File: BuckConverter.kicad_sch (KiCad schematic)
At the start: 9 parts, among them U1 TPS56339DDC

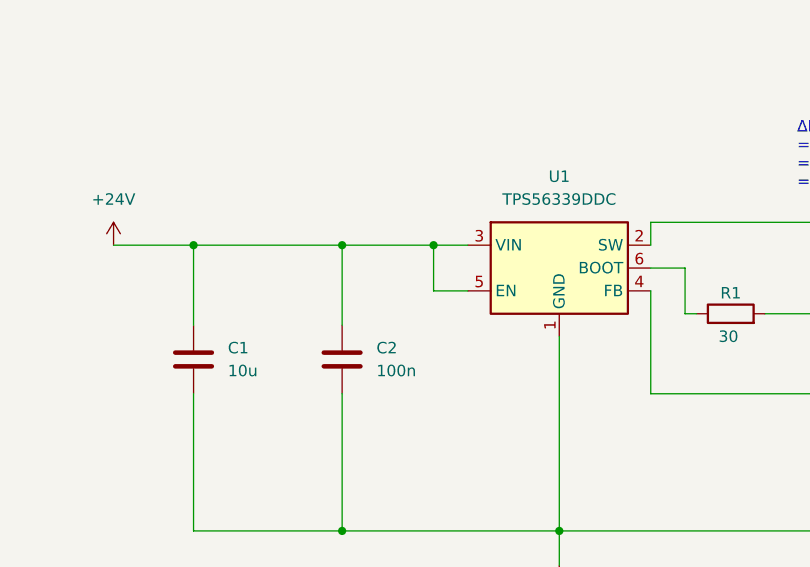
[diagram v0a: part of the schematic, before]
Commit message: added testpoints too
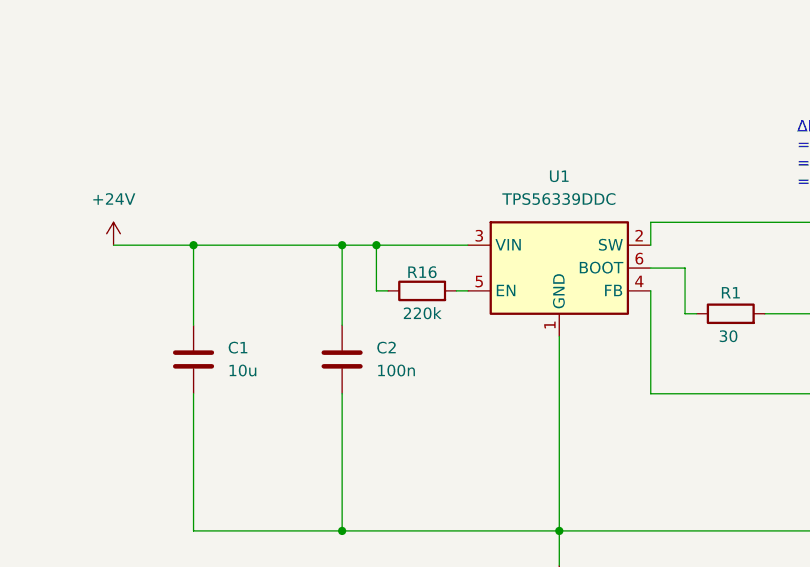
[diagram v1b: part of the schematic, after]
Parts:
- added R16: 220k, symbol Device:R
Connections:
- net +24V: now also R16.1; no longer U1.5 (EN)
- new net: R16.2, U1.5 (EN)
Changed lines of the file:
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@@
+	)
+	(junction
+		(at 104.14 72.39)
+		(diameter 0)
+		(color 0 0 0 0)
 	)
 	(junction
@@
 	)
 	(junction
-		(at 110.49 72.39)
-		(diameter 0)
-		(color 0 0 0 0)
-	)
-	(junction
 		(at 181.61 72.39)
 		(diameter 0)
@@
 	(wire
 		(pts
-			(xy 114.3 77.47) (xy 110.49 77.47)
+			(xy 114.3 77.47) (xy 113.03 77.47)
 		)
 		(stroke
@@
 	(wire
 		(pts
+			(xy 104.14 72.39) (xy 104.14 77.47)
+		)
+		(stroke
+			(width 0)
+			(type default)
+		)
+	)
+	(wire
+		(pts
 			(xy 74.93 72.39) (xy 83.82 72.39)
 		)
@@
 	(wire
 		(pts
+			(xy 104.14 72.39) (xy 114.3 72.39)
+		)
+		(stroke
+			(width 0)
+			(type default)
+		)
+	)
+	(wire
+		(pts
 			(xy 83.82 72.39) (xy 100.33 72.39)
 		)
@@
 	(wire
 		(pts
-			(xy 110.49 72.39) (xy 114.3 72.39)
-		)
-		(stroke
-			(width 0)
-			(type default)
-		)
-	)
-	(wire
-		(pts
 			(xy 162.56 80.01) (xy 162.56 74.93)
 		)
@@
 	(wire
 		(pts
-			(xy 100.33 72.39) (xy 110.49 72.39)
+			(xy 100.33 72.39) (xy 104.14 72.39)
 		)
 		(stroke
@@
 	(wire
 		(pts
+			(xy 105.41 77.47) (xy 104.14 77.47)
+		)
+		(stroke
+			(width 0)
+			(type default)
+		)
+	)
+	(wire
+		(pts
 			(xy 134.62 69.85) (xy 134.62 72.39)
 		)
@@
 		(pts
 			(xy 160.02 80.01) (xy 162.56 80.01)
-		)
-		(stroke
-			(width 0)
-			(type default)
-		)
-	)
-	(wire
-		(pts
-			(xy 110.49 77.47) (xy 110.49 72.39)
 		)
 		(stroke
@@
 					(unit 1)
 				)
+			)
+		)
+	)
+	(symbol
+		(lib_id "Device:R")
+		(at 109.22 77.47 90)
+		(unit 1)
+		(exclude_from_sim no)
+		(in_bom yes)
+		(on_board yes)
+		(dnp no)
+		(property "Reference" "R16"
+			(at 109.22 75.438 90)
+			(effects
+				(font
+					(size 1.27 1.27)
+				)
+			)
+		)
+		(property "Value" "220k"
+			(at 109.22 80.01 90)
+			(effects
+				(font
+					(size 1.27 1.27)
+				)
+			)
+		)
+		(property "Footprint" ""
+			(at 109.22 79.248 90)
+			(effects
+				(font
+					(size 1.27 1.27)
+				)
+				(hide yes)
+			)
+		)
+		(property "Datasheet" "~"
+			(at 109.22 77.47 0)
+			(effects
+				(font
+					(size 1.27 1.27)
+				)
+				(hide yes)
+			)
+		)
+		(property "Description" "Resistor"
+			(at 109.22 77.47 0)
+			(effects
+				(font
+					(size 1.27 1.27)
+				)
+				(hide yes)
+			)
+		)
+		(pin "1"
+		)
+		(pin "2"
+		)
+		(instances
+			(project ""
+				(path "/a2e13c19-ff3a-4e43-a7f5-200fd5b2b978/2c6af1c6-af26-4746-8ed9-5deb88ce0ee1"
+					(reference "R16")
+					(unit 1)
+				)

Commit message: changes + ioc
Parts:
- added C18, C3: 22u, symbol Device:C
- L1: value 20u -> 6.8u
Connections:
- net GND: now also C18.2, C3.2; no longer C17.1, L1.2, R2.1
- new net 12V_BUS: C17.1, C18.1, C3.1, L1.2, R2.1
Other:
- note removed: "L = (24-12)(12/24)/(0.8(500,000)) = 6/(400,000) = 15uH"
- note removed: "Vin = 24V Vout = 12V Fsw = 500,000 Hz (typ)"
- note removed: "Vref = .802V (typ) R9 = 10k R2 = R9(Vout - Vref)/Vref R2 = 10k(12-.802)/.802 = 140k"
- note removed: "ΔIL = 0.4(Iout) = 0.4(2A) = 0.8A"
- moved on the sheet: C1, C16, C17, C2, L1, R1, R16, R2, R9, U1

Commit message: layout
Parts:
- C1: footprint (none) -> Capacitor_SMD:C_0805_2012Metric_Pad1.18x1.45mm_HandSolder; Manufacturer_Part_Number (none) -> GRM21BR61H106KE43K
- C16, C2: footprint (none) -> Capacitor_SMD:C_0603_1608Metric_Pad1.08x0.95mm_HandSolder; Manufacturer_Part_Number (none) -> MLASH168SB7104KTNA01
- C17, C18, C3: footprint (none) -> Capacitor_SMD:C_0805_2012Metric_Pad1.18x1.45mm_HandSolder
- L1: footprint (none) -> Inductor_SMD:L_6.3x6.3_H3
- R1, R16, R2: footprint (none) -> Resistor_SMD:R_0603_1608Metric_Pad0.98x0.95mm_HandSolder
- R9: footprint (none) -> Resistor_SMD:R_0603_1608Metric_Pad0.98x0.95mm_HandSolder; Manufacturer_Part_Number (none) -> CRCW060310K0FKEI

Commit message: hello
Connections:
- net SW: now reaches C16.2, L1.1, U1.2 (SW)
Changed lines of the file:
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@@
+		)
+	)
+	(label "SW"
+		(at 132.08 92.71 0)
+		(effects
+			(font
+				(size 1.27 1.27)
+			)
+			(justify left bottom)
 		)
 	)

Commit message: done
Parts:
- L1: Mouser Part Number (none) -> 80-MPEV1D0630L6R8
- U1: Mouser Part Number (none) -> 595-TPS56339DDCR
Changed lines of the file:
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@@
+			)
+		)
+		(property "Sim.Type" ""
+			(at 175.26 115.57 0)
+			(effects
+				(font
+					(size 1.27 1.27)
+				)
+				(hide yes)
 			)
 		)
@@
 			)
 		)
+		(property "Sim.Type" ""
+			(at 93.98 107.95 0)
+			(effects
+				(font
+					(size 1.27 1.27)
+				)
+				(hide yes)
+			)
+		)
 		(pin "1"
 		)
@@
 		)
 		(property "Mouser Link" ""
+			(at 102.87 100.33 90)
+			(effects
+				(font
+					(size 1.27 1.27)
+				)
+				(hide yes)
+			)
+		)
+		(property "Sim.Type" ""
 			(at 102.87 100.33 90)
 			(effects
@@
 			)
 		)
+		(property "Sim.Type" ""
+			(at 175.26 102.87 0)
+			(effects
+				(font
+					(size 1.27 1.27)
+				)
+				(hide yes)
+			)
+		)
 		(pin "1"
 		)
@@
 			)
 		)
+		(property "Sim.Type" ""
+			(at 190.5 107.95 0)
+			(effects
+				(font
+					(size 1.27 1.27)
+				)
+				(hide yes)
+			)
+		)
 		(pin "1"
 		)
@@
 			)
 		)
+		(property "Sim.Type" ""
+			(at 215.9 107.95 0)
+			(effects
+				(font
+					(size 1.27 1.27)
+				)
+				(hide yes)
+			)
+		)
 		(pin "1"
 		)
@@
 			)
 		)
+		(property "Sim.Type" ""
+			(at 137.16 100.33 90)
+			(effects
+				(font
+					(size 1.27 1.27)
+				)
+				(hide yes)
+			)
+		)
 		(pin "2"
 		)
@@
 			)
 		)
+		(property "Sim.Type" ""
+			(at 118.11 97.79 0)
+			(effects
+				(font
+					(size 1.27 1.27)
+				)
+				(hide yes)
+			)
+		)
+		(property "Mouser Part Number" "595-TPS56339DDCR"
+			(at 118.11 97.79 0)
+			(effects
+				(font
+					(size 1.27 1.27)
+				)
+				(hide yes)
+			)
+		)
 		(pin "5"
 		)
@@
 			)
 		)
+		(property "Sim.Type" ""
+			(at 77.47 107.95 0)
+			(effects
+				(font
+					(size 1.27 1.27)
+				)
+				(hide yes)
+			)
+		)
 		(pin "1"
 		)
@@
 			)
 		)
+		(property "Sim.Type" ""
+			(at 203.2 107.95 0)
+			(effects
+				(font
+					(size 1.27 1.27)
+				)
+				(hide yes)
+			)
+		)
 		(pin "1"
 		)
@@
 			)
 		)
-		(property "Datasheet" "~"
+		(property "Datasheet" ""
 			(at 163.83 97.79 0)
 			(effects
@@
 		)
 		(property "Mouser Link" ""
+			(at 163.83 97.79 90)
+			(effects
+				(font
+					(size 1.27 1.27)
+				)
+				(hide yes)
+			)
+		)
+		(property "Sim.Type" ""
+			(at 163.83 97.79 90)
+			(effects
+				(font
+					(size 1.27 1.27)
+				)
+				(hide yes)
+			)
+		)
+		(property "Mouser Part Number" "80-MPEV1D0630L6R8"
 			(at 163.83 97.79 90)
 			(effects
@@
 			(at 149.86 100.33 90)
 			(effects
+				(font
+					(size 1.27 1.27)
+				)
+				(hide yes)
+			)
+		)
+		(property "Sim.Type" ""
+			(at 149.86 100.33 90)
+			(effects
